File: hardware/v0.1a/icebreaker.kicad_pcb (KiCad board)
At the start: 4 copper layers, 73 x 37 mm, 115 parts, among them J1 Jumper, J10 Jumper, J11 Jumper, J12 Jumper, J13 Jumper, J14 Jumper, J15 Jumper, J16 Jumper, J17 Jumper, J18 Jumper, J19 Jumper, J2 Jumper, J20 Flash, J21 PMOD_1A, J22 PMOD_1B, J23 PMOD_2H, J24 PMOD_2P, J25 RGB Led, J26 5V AUX, J27 5V AUX, J3 Jumper, J4 Jumper, J5 Jumper, J6 Jumper, J7 Jumper, J8 Jumper, J9 Jumper, P1 pkl_USB_OTG, SW1 TACT, SW2 TACT, SW3 TACT, SW4 TACT, U1 93C46B-SOT-23-6, U2 3.3V, U3 1V2, U4 FT2232H, U5 W25Q, U6 ICE5LP4K-SG48, X1 12MHz

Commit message: Fixed pin header 3d models.
We had some of the models doubled up or not fully disabled. Now the TH
pin headers are all using KiCad V5 3d model locations and are all
disabled.

This fixes #23
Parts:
- removed the REF** at (38.6, 47.1)
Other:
- board text removed: "1Bitsquared"

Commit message: Added more legend silkscreen to ears.
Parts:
- added REF**: 1b2_Logo_SilkS_5mm, pkl_logos:1b2_Logo_SilkS_5mm, B.Cu at (38.6, 47.1)
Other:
- board text added: "1Bitsquared"
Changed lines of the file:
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@@
   (general
     (thickness 1.6)
-    (drawings 94)
+    (drawings 95)
     (tracks 1324)
     (zones 0)
-    (modules 114)
+    (modules 115)
     (nets 100)
   )
@@
     (add_net "Net-(U4-Pad60)")
   )
+  (module pkl_logos:1b2_Logo_SilkS_5mm locked (layer B.Cu)
+    (at 38.6 47.1 180)
+    (fp_text reference REF** (at 0 -4 180) (layer B.Fab) hide
+      (effects (font (size 1 1) (thickness 0.15)) (justify mirror))
+    )
+    (fp_text value 1b2_Logo_SilkS_5mm (at 0 4 180) (layer B.Fab) hide
+      (effects (font (size 1 1) (thickness 0.15)) (justify mirror))
+    )
+    (fp_line (start -0.5 0.5) (end -0.5 2.5) (layer B.SilkS) (width 0.2))
+    (fp_line (start -0.5 2.5) (end -2.5 2.5) (layer B.SilkS) (width 0.2))
+    (fp_line (start -2.5 2.5) (end -2.5 0.5) (layer B.SilkS) (width 0.2))
+    (fp_line (start -2.5 0.5) (end -0.5 0.5) (layer B.SilkS) (width 0.2))
+    (fp_line (start -0.5 2.5) (end 0 2) (layer B.SilkS) (width 0.2))
+    (fp_line (start 0 2) (end 0 0) (layer B.SilkS) (width 0.2))
+    (fp_line (start 0 0) (end -0.5 0.5) (layer B.SilkS) (width 0.2))
+    (fp_line (start -2.5 0.5) (end -2 0) (layer B.SilkS) (width 0.2))
+    (fp_line (start -2 0) (end 0 0) (layer B.SilkS) (width 0.2))
+    (fp_line (start 2 2) (end 0.5 2) (layer B.SilkS) (width 0.2))
+    (fp_line (start 0.5 2) (end 0.5 -0.5) (layer B.SilkS) (width 0.2))
+    (fp_line (start 0.5 -0.5) (end -2 -0.5) (layer B.SilkS) (width 0.2))
+    (fp_line (start -2 -0.5) (end -2 -2) (layer B.SilkS) (width 0.2))
+    (fp_line (start -2 -2) (end 2 -2) (layer B.SilkS) (width 0.2))
+    (fp_line (start 2 -2) (end 2 2) (layer B.SilkS) (width 0.2))
+    (fp_line (start 2 2) (end 2.5 1.5) (layer B.SilkS) (width 0.2))
+    (fp_line (start 2.5 1.5) (end 2.5 -2.5) (layer B.SilkS) (width 0.2))
+    (fp_line (start 2.5 -2.5) (end 2 -2) (layer B.SilkS) (width 0.2))
+    (fp_line (start -2 -2) (end -1.5 -2.5) (layer B.SilkS) (width 0.2))
+    (fp_line (start -1.5 -2.5) (end 2.5 -2.5) (layer B.SilkS) (width 0.2))
+  )
   (module pkl_jumpers:J_0603 (layer B.Cu)
     (at 51.4 43.35)
@@
       (net 1 /Rx_TTL/FIFO_D0))
   )
+  (gr_text 1Bitsquared (at 38.5 50.9) (layer B.SilkS)
+    (effects (font (size 1 1) (thickness 0.25)) (justify mirror))
+  )
   (gr_text "(C) 2018\n1Bitsquared" (at 57.4 40.9) (layer F.SilkS)

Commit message: Replaced/added the null logo to the boards.
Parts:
- REF**: value 1b2_Logo_SilkS_5mm -> null_Logo_SilkS_5mm; footprint pkl_logos:1b2_Logo_SilkS_5mm -> pkl_logos:null_Logo_SilkS_5mm
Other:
- board text added: "NULL"
- board text removed: "1Bitsquared"
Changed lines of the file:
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@@
-(kicad_pcb (version 20171130) (host pcbnew 5.1.2-f72e74a~84~ubuntu18.04.1)
+(kicad_pcb (version 20171130) (host pcbnew 5.1.5-52549c5~86~ubuntu19.10.1)
   (general
     (thickness 1.6)
@@
     (add_net "Net-(U4-Pad60)")
   )
-  (module pkl_logos:1b2_Logo_SilkS_5mm locked (layer B.Cu)
+  (module pkl_logos:null_Logo_SilkS_5mm locked (layer B.Cu)
     (at 38.6 47.1 180)
     (fp_text reference REF** (at 0 -4 180) (layer B.Fab) hide
       (effects (font (size 1 1) (thickness 0.15)) (justify mirror))
     )
-    (fp_text value 1b2_Logo_SilkS_5mm (at 0 4 180) (layer B.Fab) hide
+    (fp_text value null_Logo_SilkS_5mm (at 0 4 180) (layer B.Fab) hide
       (effects (font (size 1 1) (thickness 0.15)) (justify mirror))
     )
-    (fp_line (start -0.5 0.5) (end -0.5 2.5) (layer B.SilkS) (width 0.2))
-    (fp_line (start -0.5 2.5) (end -2.5 2.5) (layer B.SilkS) (width 0.2))
-    (fp_line (start -2.5 2.5) (end -2.5 0.5) (layer B.SilkS) (width 0.2))
-    (fp_line (start -2.5 0.5) (end -0.5 0.5) (layer B.SilkS) (width 0.2))
-    (fp_line (start -0.5 2.5) (end 0 2) (layer B.SilkS) (width 0.2))
-    (fp_line (start 0 2) (end 0 0) (layer B.SilkS) (width 0.2))
-    (fp_line (start 0 0) (end -0.5 0.5) (layer B.SilkS) (width 0.2))
-    (fp_line (start -2.5 0.5) (end -2 0) (layer B.SilkS) (width 0.2))
-    (fp_line (start -2 0) (end 0 0) (layer B.SilkS) (width 0.2))
-    (fp_line (start 2 2) (end 0.5 2) (layer B.SilkS) (width 0.2))
-    (fp_line (start 0.5 2) (end 0.5 -0.5) (layer B.SilkS) (width 0.2))
-    (fp_line (start 0.5 -0.5) (end -2 -0.5) (layer B.SilkS) (width 0.2))
-    (fp_line (start -2 -0.5) (end -2 -2) (layer B.SilkS) (width 0.2))
-    (fp_line (start -2 -2) (end 2 -2) (layer B.SilkS) (width 0.2))
-    (fp_line (start 2 -2) (end 2 2) (layer B.SilkS) (width 0.2))
-    (fp_line (start 2 2) (end 2.5 1.5) (layer B.SilkS) (width 0.2))
-    (fp_line (start 2.5 1.5) (end 2.5 -2.5) (layer B.SilkS) (width 0.2))
-    (fp_line (start 2.5 -2.5) (end 2 -2) (layer B.SilkS) (width 0.2))
-    (fp_line (start -2 -2) (end -1.5 -2.5) (layer B.SilkS) (width 0.2))
-    (fp_line (start -1.5 -2.5) (end 2.5 -2.5) (layer B.SilkS) (width 0.2))
+    (fp_arc (start -0.4 -0.2) (end -0.7 -0.2) (angle 180) (layer B.SilkS) (width 0.15))
+    (fp_line (start 1 -0.5) (end 1.5 -0.5) (layer B.SilkS) (width 0.15))
+    (fp_line (start 1 0.5) (end 1 -0.5) (layer B.SilkS) (width 0.15))
+    (fp_line (start 0.2 -0.5) (end 0.7 -0.5) (layer B.SilkS) (width 0.15))
+    (fp_line (start 0.2 0.5) (end 0.2 -0.5) (layer B.SilkS) (width 0.15))
+    (fp_line (start -0.1 0.5) (end -0.1 -0.2) (layer B.SilkS) (width 0.15))
+    (fp_line (start -0.7 0.5) (end -0.7 -0.2) (layer B.SilkS) (width 0.15))
+    (fp_line (start -1 -0.5) (end -1 0.5) (layer B.SilkS) (width 0.15))
+    (fp_line (start -1.5 0.5) (end -1 -0.5) (layer B.SilkS) (width 0.15))
+    (fp_line (start -1.5 -0.5) (end -1.5 0.5) (layer B.SilkS) (width 0.15))
+    (fp_line (start 2.5 2.5) (end -2.5 2.5) (layer B.SilkS) (width 0.2))
+    (fp_line (start -2.5 2.5) (end -2.5 -2.5) (layer B.SilkS) (width 0.2))
+    (fp_line (start 2.5 2.5) (end 2.5 -2.5) (layer B.SilkS) (width 0.2))
+    (fp_line (start -2.5 -2.5) (end 2.5 -2.5) (layer B.SilkS) (width 0.2))
   )
   (module pkl_jumpers:J_0603 (layer B.Cu)
@@
       (net 1 /Rx_TTL/FIFO_D0))
   )
-  (gr_text 1Bitsquared (at 38.5 50.9) (layer B.SilkS)
+  (gr_text NULL (at 38.5 50.9) (layer B.SilkS)
     (effects (font (size 1 1) (thickness 0.25)) (justify mirror))
   )

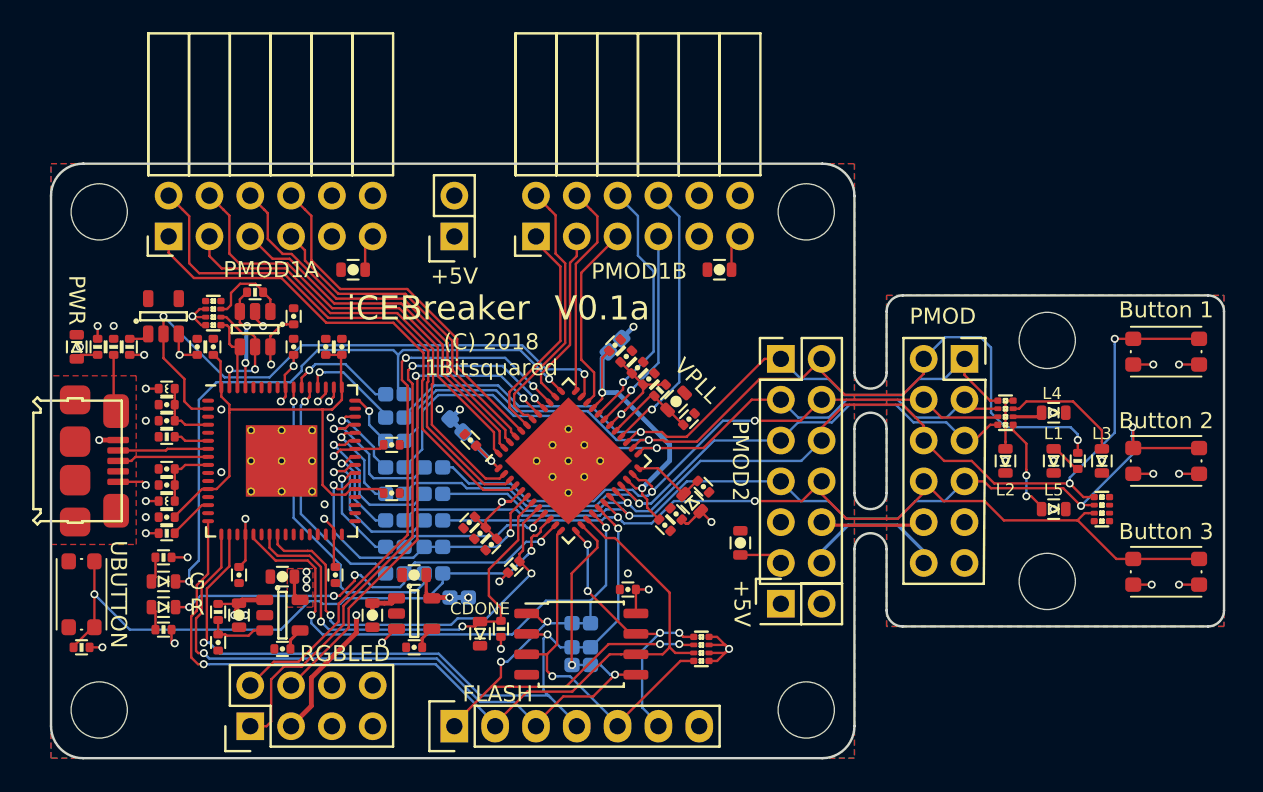
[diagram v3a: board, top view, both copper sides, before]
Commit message: Updated all design files to KiCad V8.0.6.
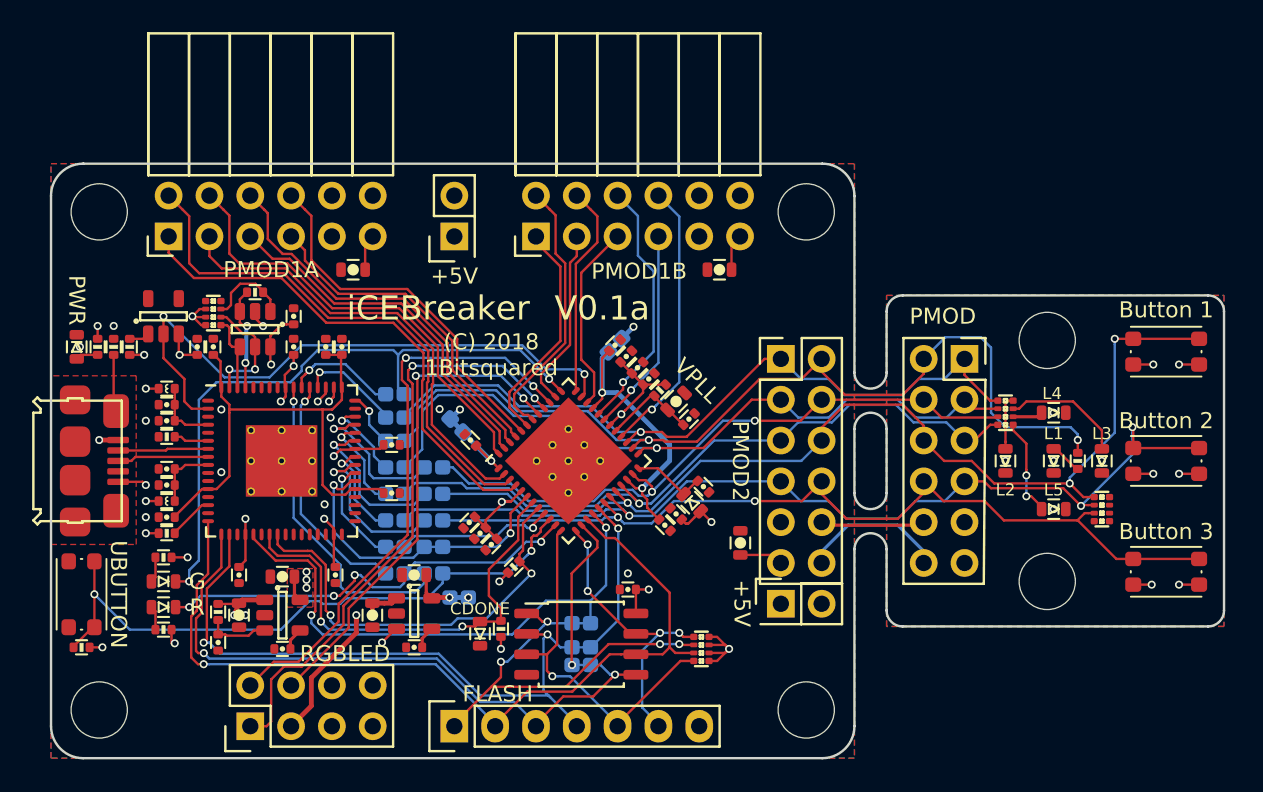
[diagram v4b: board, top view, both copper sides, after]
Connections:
- net /FLASH_~HLD~/~RST~/IO3 renamed /FLASH_~{HLD}/~{RST}/IO3
- net /FLASH_~WP~/IO2 renamed /FLASH_~{WP}/IO2
- net /xFIFO_~RD renamed /xFIFO_~{RD}
- net /xFIFO_~RXF renamed /xFIFO_~{RXF}
- net /xFIFO_~TXE renamed /xFIFO_~{TXE}
- net /xFIFO_~WR renamed /xFIFO_~{WR}
- net /~BUTTON renamed /~{BUTTON}
- net /~LEDG renamed /~{LEDG}
- net /~LEDR renamed /~{LEDR}
- net /~LED_BLU renamed /~{LED_BLU}
- net /~LED_GRN renamed /~{LED_GRN}
- net /~LED_RED renamed /~{LED_RED}
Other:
- net class Default removed
